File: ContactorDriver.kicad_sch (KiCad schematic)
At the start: 30 parts, among them Con1 LED, Con2 LED, Con3 LED, J4 Conn_01x04, J5 Conn_01x04, J6 Conn_01x04, Q4 IRLML0030, Q5 IRLML0030, Q6 IRLML0030

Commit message: initial commit post VCU block diagram
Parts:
- removed A_Pre_Sen_TP1: TestPoint, utsvt-special:TestPoint_HEX_3mmID, symbol Connector:TestPoint
- removed C19: 0.1u, Capacitor_SMD:C_0805_2012Metric, symbol Device:C
- removed Con2: LED, LED_SMD:LED_0805_2012Metric, symbol Device:LED
- removed D9: D, Active-PrechargeLib:SODFL4724X108N, symbol Device:D
- removed J5: Conn_01x04, utsvt-conn:Molex_MicroFit3.0_1x4xP3.00mm_PolarizingPeg_Vertical, symbol Connector_Generic:Conn_01x04
- removed Q5: IRLML0030, Package_TO_SOT_SMD:SOT-23, symbol Transistor_FET:IRLML0030
- removed R22, R31: 10k, Resistor_SMD:R_0805_2012Metric, symbol Device:R_US
- removed R23: 2k, Resistor_SMD:R_0805_2012Metric, symbol Device:R_US
- removed R30: 30k, Resistor_SMD:R_0805_2012Metric, symbol Device:R_US
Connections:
- net LVGND renamed GND
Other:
- note removed: "Array Precharge Coil+"
- note removed: "Array Precharge Contactor Driver"
- note removed: "Array Precharge Contactor Indicator LED"

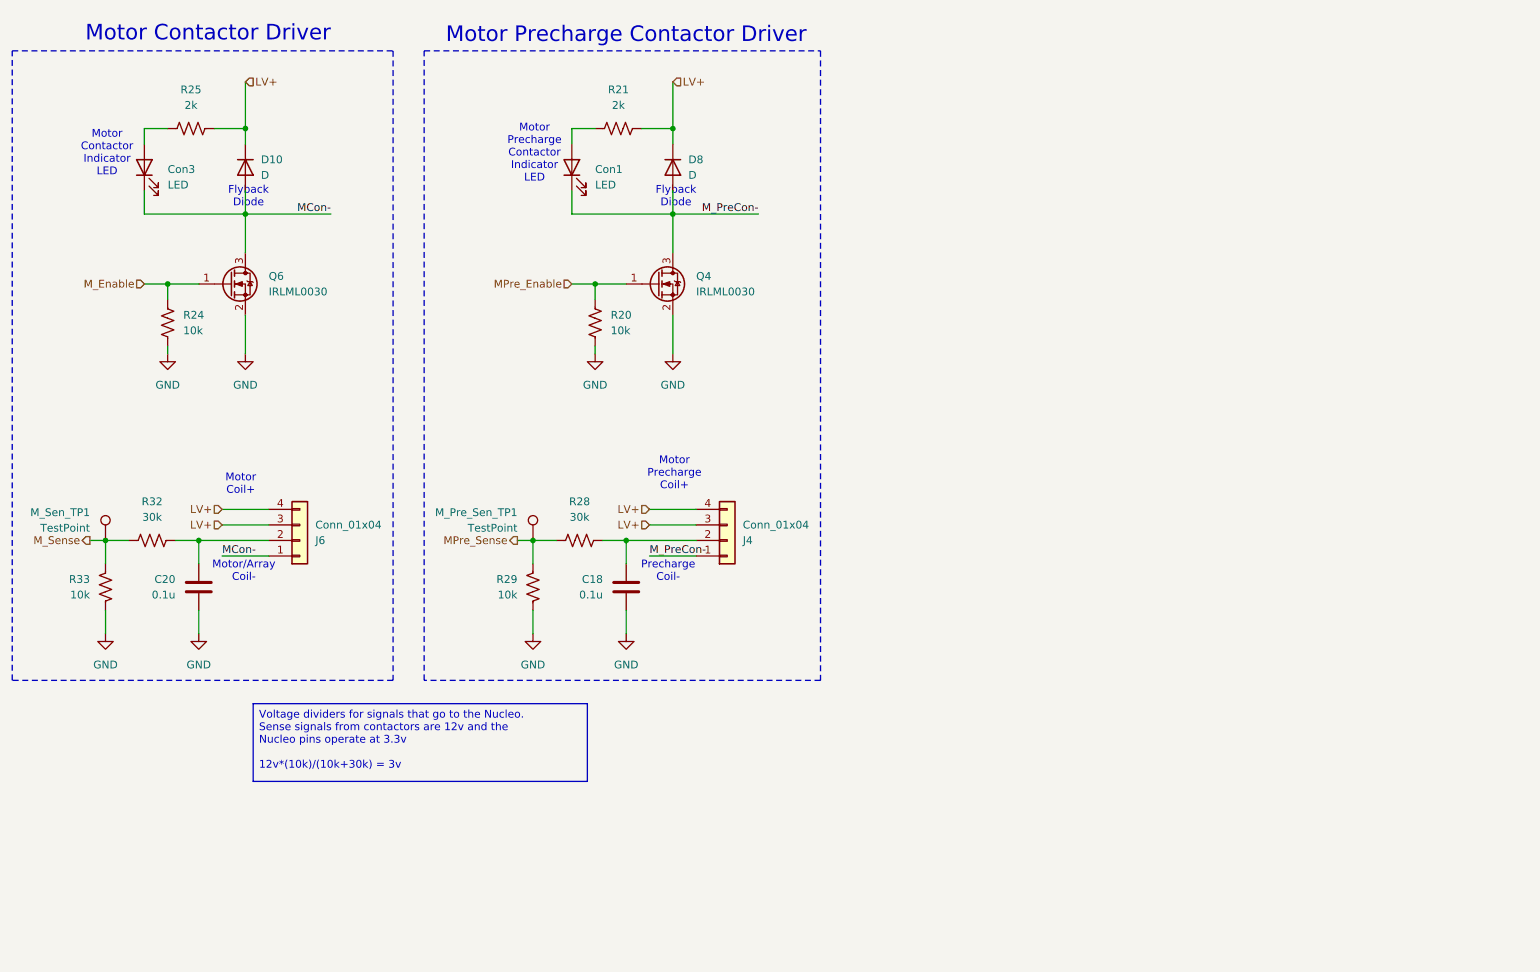
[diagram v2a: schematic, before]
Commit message: added opto's to sense signals
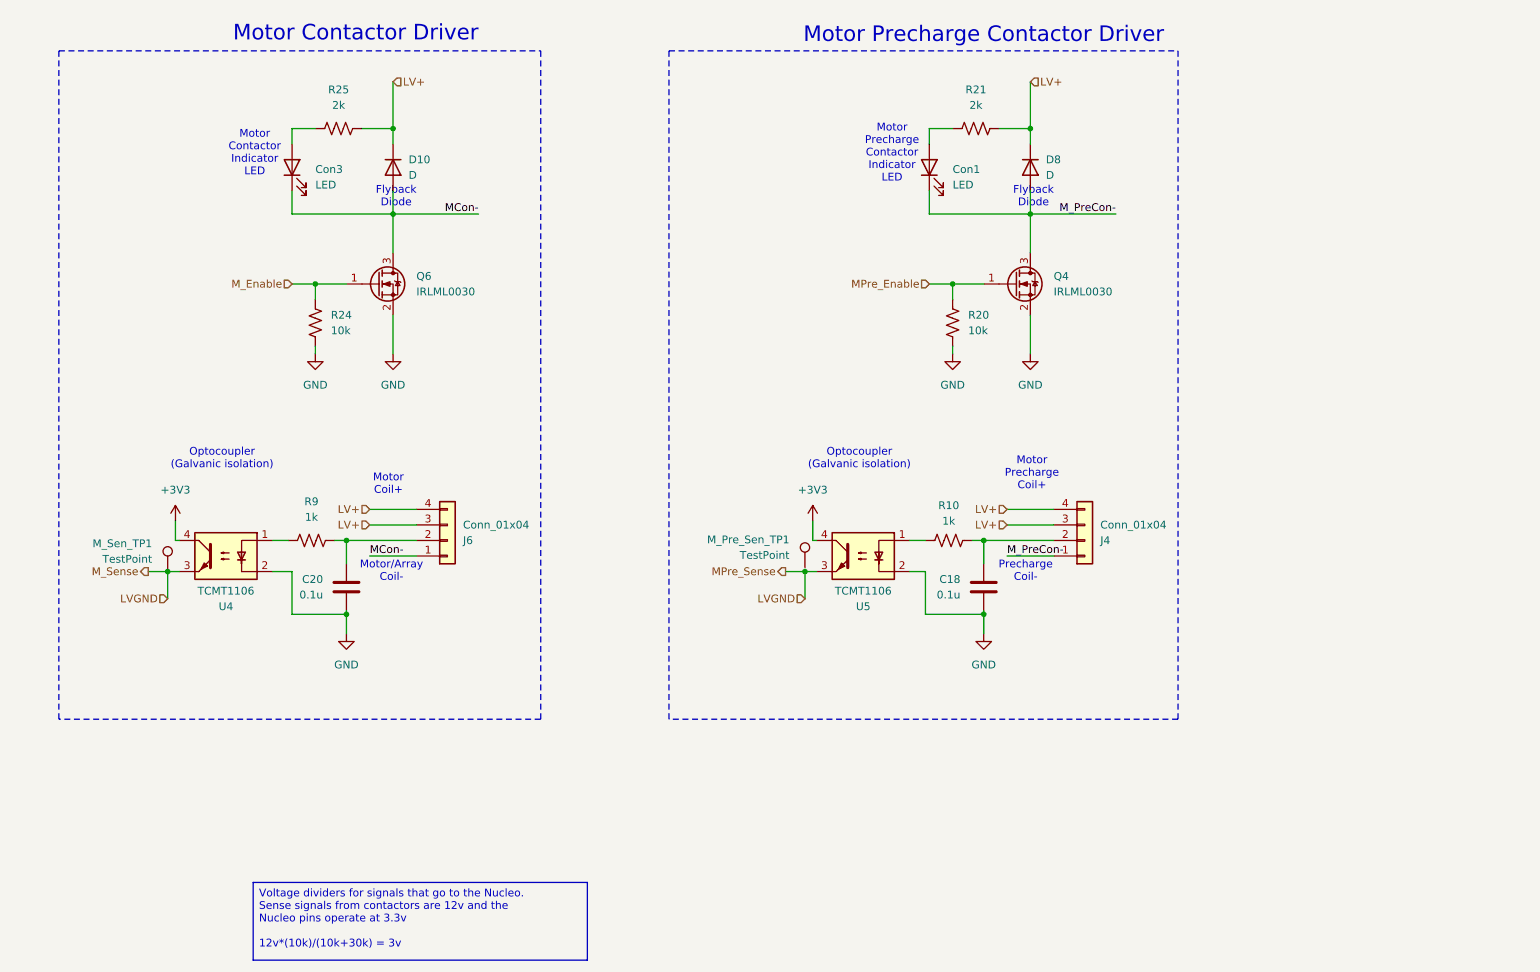
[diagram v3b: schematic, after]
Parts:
- removed R28, R32: 30k, Resistor_SMD:R_0805_2012Metric, symbol Device:R_US
- removed R29, R33: 10k, Resistor_SMD:R_0805_2012Metric, symbol Device:R_US
- added R10, R9: 1k, Resistor_SMD:R_0805_2012Metric, symbol Device:R_US
- added U4, U5: TCMT1106, Package_SO:SOP-4_4.4x2.6mm_P1.27mm, symbol Isolator:TCMT1106
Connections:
- net GND: now also U4.2, U5.2
- net at C18.1, J4.2 (Pin_2): now also R10.1
- net at C20.1, J6.2 (Pin_2): now also R9.1
- net MPre_Sense: no longer names the net of M_Pre_Sen_TP1.1
- net M_Sense renamed LVGND
- net LVGND: now also U4.3, U5.3
- new net: R9.2, U4.1
- new net: R10.2, U5.1
- new net +3V3: U4.4, U5.4
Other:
- note added: "Optocoupler (Galvanic isolation)"
- moved on the sheet: C18, C20, Con1, Con3, D10, D8, J4, J6, M_Pre_Sen_TP1, Q4, Q6, R20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

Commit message: layout start
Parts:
- added C11, C13: 1u, Capacitor_SMD:C_0805_2012Metric, symbol Device:C
- added R15, R20: 10k, Resistor_SMD:R_0805_2012Metric, symbol Device:R_US
- added R16, R21: 100, Resistor_SMD:R_0805_2012Metric, symbol Device:R_US
- J14: renamed from J6; footprint utsvt-conn:Molex_MicroFit3.0_1x4xP3.00mm_PolarizingPeg_Vertical -> utsvt_conn:Molex_MicroFit3.0_1x4xP3.00mm_PolarizingPeg_Vertical
- J15: renamed from J4; footprint utsvt-conn:Molex_MicroFit3.0_1x4xP3.00mm_PolarizingPeg_Vertical -> utsvt_conn:Molex_MicroFit3.0_1x4xP3.00mm_PolarizingPeg_Vertical
- M_Pre_Sen_TP1, M_Sen_TP1: footprint utsvt-special:TestPoint_HEX_3mmID -> UTSVT_Special:TestPoint_HEX_3mmID
- renumbered C20 to C12, C18 to C14, Con3 to Con1, Con1 to Con2, D10 to D8, D8 to D9, Q6 to Q2, Q4 to Q3, R9 to R17, R24 to R18, R25 to R19, R10 to R22, R20 to R23, R21 to R24
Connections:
- net LVGND: now also C11.1, C13.1, R15.2, R20.2; no longer M_Sen_TP1.1, U4.3, U5.3
- net MPre_Sense: now reaches M_Pre_Sen_TP1.1
- net MPre_Sense: now also C13.2, R20.1, R21.1
- net +3V3 renamed 3V3_LSOM
- new net: R21.2, U5.3
- new net: R16.2, U4.3
- new net M_Sense: C11.2, M_Sen_TP1.1, R15.1, R16.1
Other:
- moved on the sheet: C12, C14, Con1, Con2, D8, D9, J14, J15, M_Sen_TP1, Q2, Q3, R17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

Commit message: first revision
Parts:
- renumbered C11 to C12, C12 to C13, C13 to C14, C14 to C15, D9 to D10, D8 to D9
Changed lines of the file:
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@@
 		(dnp no)
 		(fields_autoplaced yes)
-		(property "Reference" "C11"
+		(property "Reference" "C12"
 			(at 59.055 117.4749 0)
 			(effects
@@
 			(project ""
 				(path "/795c8e51-3ded-4d21-b864-aaff31c5def7/838dfc75-afcf-4845-8c43-fcef4e0ee00c"
-					(reference "C11")
+					(reference "C12")
 					(unit 1)
 				)
@@
 		(dnp no)
 		(fields_autoplaced yes)
-		(property "Reference" "C13"
+		(property "Reference" "C14"
 			(at 179.705 118.1099 0)
 			(effects
@@
 			(project "VehicleControlUnit"
 				(path "/795c8e51-3ded-4d21-b864-aaff31c5def7/838dfc75-afcf-4845-8c43-fcef4e0ee00c"
-					(reference "C13")
+					(reference "C14")
 					(unit 1)
 				)
@@
 		(dnp no)
 		(fields_autoplaced yes)
-		(property "Reference" "D8"
+		(property "Reference" "D9"
 			(at 114.935 43.8149 90)
 			(effects
@@
 			(project "VehicleControlUnit"
 				(path "/795c8e51-3ded-4d21-b864-aaff31c5def7/838dfc75-afcf-4845-8c43-fcef4e0ee00c"
-					(reference "D8")
+					(reference "D9")
 					(unit 1)
 				)
@@
 		(dnp no)
 		(fields_autoplaced yes)
-		(property "Reference" "#PWR043"
+		(property "Reference" "#PWR045"
 			(at 226.695 128.27 0)
 			(effects
@@
 			(project "VehicleControlUnit"
 				(path "/795c8e51-3ded-4d21-b864-aaff31c5def7/838dfc75-afcf-4845-8c43-fcef4e0ee00c"
-					(reference "#PWR043")
+					(reference "#PWR045")
 					(unit 1)
 				)
@@
 		(dnp no)
 		(fields_autoplaced yes)
-		(property "Reference" "#PWR042"
+		(property "Reference" "#PWR044"
 			(at 221.615 82.55 0)
 			(effects
@@
 			(project "VehicleControlUnit"
 				(path "/795c8e51-3ded-4d21-b864-aaff31c5def7/838dfc75-afcf-4845-8c43-fcef4e0ee00c"
-					(reference "#PWR042")
+					(reference "#PWR044")
 					(unit 1)
 				)
@@
 		(dnp no)
 		(fields_autoplaced yes)
-		(property "Reference" "#PWR044"
+		(property "Reference" "#PWR046"
 			(at 234.315 82.55 0)
 			(effects
@@
 			(project "VehicleControlUnit"
 				(path "/795c8e51-3ded-4d21-b864-aaff31c5def7/838dfc75-afcf-4845-8c43-fcef4e0ee00c"
-					(reference "#PWR044")
+					(reference "#PWR046")
 					(unit 1)
 				)
@@
 		(on_board yes)
 		(dnp no)
-		(property "Reference" "C12"
+		(property "Reference" "C13"
 			(at 100.965 112.3949 0)
 			(effects
@@
 			(project "VehicleControlUnit"
 				(path "/795c8e51-3ded-4d21-b864-aaff31c5def7/838dfc75-afcf-4845-8c43-fcef4e0ee00c"
-					(reference "C12")
+					(reference "C13")
 					(unit 1)
 				)
@@
 		(dnp no)
 		(fields_autoplaced yes)
-		(property "Reference" "#PWR041"
+		(property "Reference" "#PWR043"
 			(at 112.395 81.915 0)
 			(effects
@@
 			(project "VehicleControlUnit"
 				(path "/795c8e51-3ded-4d21-b864-aaff31c5def7/838dfc75-afcf-4845-8c43-fcef4e0ee00c"
-					(reference "#PWR041")
+					(reference "#PWR043")
 					(unit 1)
 				)
@@
 		(dnp no)
 		(fields_autoplaced yes)
-		(property "Reference" "#PWR040"
+		(property "Reference" "#PWR042"
 			(at 104.775 127.635 0)
 			(effects
@@
 			(project "VehicleControlUnit"
 				(path "/795c8e51-3ded-4d21-b864-aaff31c5def7/838dfc75-afcf-4845-8c43-fcef4e0ee00c"
-					(reference "#PWR040")
+					(reference "#PWR042")
 					(unit 1)
 				)
@@
 		(dnp no)
 		(fields_autoplaced yes)
-		(property "Reference" "#PWR039"
+		(property "Reference" "#PWR041"
 			(at 99.695 81.915 0)
 			(effects
@@
 			(project "VehicleControlUnit"
 				(path "/795c8e51-3ded-4d21-b864-aaff31c5def7/838dfc75-afcf-4845-8c43-fcef4e0ee00c"
-					(reference "#PWR039")
+					(reference "#PWR041")
 					(unit 1)
 				)
@@
 		(on_board yes)
 		(dnp no)
-		(property "Reference" "C14"
+		(property "Reference" "C15"
 			(at 222.885 113.0299 0)
 			(effects
@@
 			(project "VehicleControlUnit"
 				(path "/795c8e51-3ded-4d21-b864-aaff31c5def7/838dfc75-afcf-4845-8c43-fcef4e0ee00c"
-					(reference "C14")
+					(reference "C15")
 					(unit 1)
 				)
@@
 		(dnp no)
 		(fields_autoplaced yes)
-		(property "Reference" "D9"
+		(property "Reference" "D10"
 			(at 236.855 44.4499 90)
 			(effects
@@
 			(project "VehicleControlUnit"
 				(path "/795c8e51-3ded-4d21-b864-aaff31c5def7/838dfc75-afcf-4845-8c43-fcef4e0ee00c"
-					(reference "D9")
-					(unit 1)
-				)
+					(reference "D10")
+					(unit 1)
+				)

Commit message: tweaking
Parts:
- R17, R22: value 1k -> 2k
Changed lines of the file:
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@@
 		(fields_autoplaced yes)
 		(property "Reference" "R17"
-			(at 99.06 99.695 90)
-			(effects
-				(font
-					(size 1.27 1.27)
-				)
-			)
-		)
-		(property "Value" "1k"
-			(at 99.06 102.235 90)
+			(at 99.06 100.33 90)
+			(effects
+				(font
+					(size 1.27 1.27)
+				)
+			)
+		)
+		(property "Value" "2k"
+			(at 99.06 102.87 90)
 			(effects
 				(font
@@
 			)
 		)
-		(property "Value" "1k"
+		(property "Value" "2k"
 			(at 220.98 103.505 90)
 			(effects

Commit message: fixed
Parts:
- renumbered C12 to C11, C13 to C12, C14 to C13, C15 to C14, D9 to D8, D10 to D9
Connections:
- net LVGND is gone; now on net GND: C11.1, C13.1, R15.2, R20.2

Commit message: review changes
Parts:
- renumbered J14 to J13, J15 to J14
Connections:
- net LV+ renamed +12V
